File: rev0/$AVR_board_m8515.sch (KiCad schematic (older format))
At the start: 18 parts, among them IC1 ATMEGA8515-A, IC2 ATMEGA8515-M, K1 SERIAL, P1 FTDI_HEADER, P2 LEFT_HEADER, P3 CONN_3X2, P4 RIGHT_HEADER, SW1 SW_PUSH, X1 CRYSTAL_TH, X2 CRYSTAL_SMD

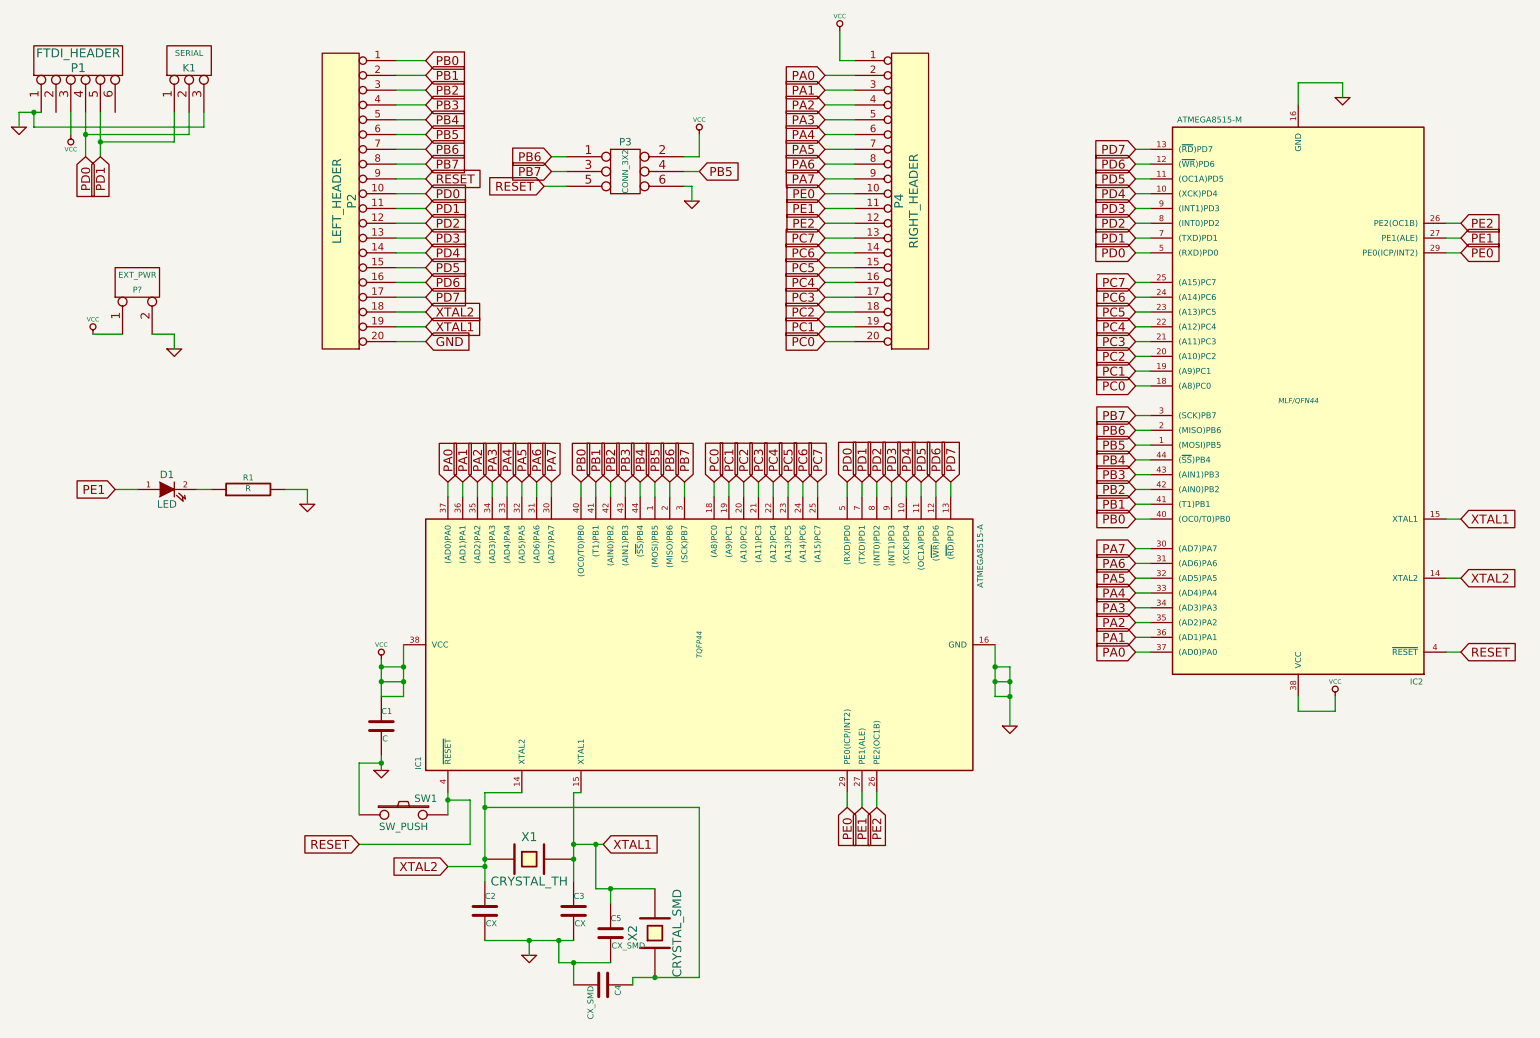
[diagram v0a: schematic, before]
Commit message: added logo mod file, also added silkscreen refs
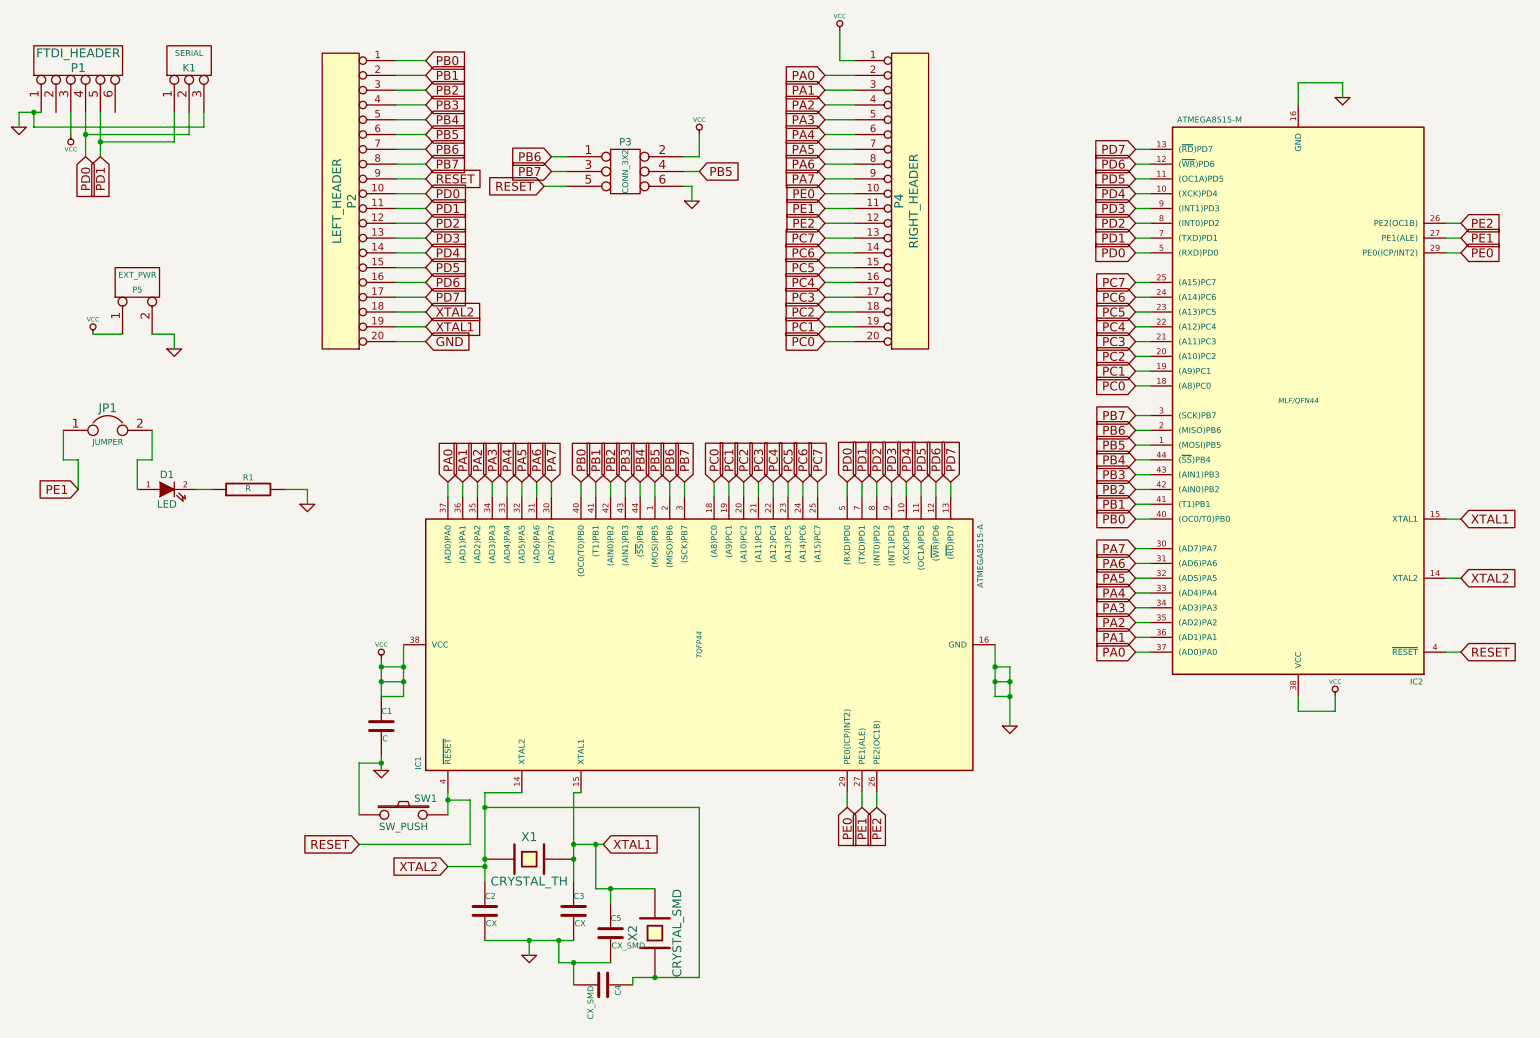
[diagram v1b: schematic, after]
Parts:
- added JP1: JUMPER, symbol JUMPER
- gave numbers to parts that had none: 1
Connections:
- net PE1: now also JP1.1; no longer D1.1 (A)
- new net: D1.1 (A), JP1.2
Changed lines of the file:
@@
 $EndComp
 $Comp
-L GND #PWR01
+L GND #PWR8
 U 1 1 54186B5E
 P 4500 7050
-F 0 "#PWR01" H 4500 7050 30  0001 C CNN
+F 0 "#PWR8" H 4500 7050 30  0001 C CNN
 F 1 "GND" H 4500 6980 30  0001 C CNN
 F 2 "" H 4500 7050 60  0000 C CNN
@@
 $EndComp
 $Comp
-L GND #PWR02
+L GND #PWR7
 U 1 1 54186C19
 P 3500 5800
-F 0 "#PWR02" H 3500 5800 30  0001 C CNN
+F 0 "#PWR7" H 3500 5800 30  0001 C CNN
 F 1 "GND" H 3500 5730 30  0001 C CNN
 F 2 "" H 3500 5800 60  0000 C CNN
@@
 $EndComp
 $Comp
-L VCC #PWR03
+L VCC #PWR6
 U 1 1 54186C37
 P 3500 5050
-F 0 "#PWR03" H 3500 5150 30  0001 C CNN
+F 0 "#PWR6" H 3500 5150 30  0001 C CNN
 F 1 "VCC" H 3500 5150 30  0000 C CNN
 F 2 "" H 3500 5050 60  0000 C CNN
@@
 	3500 5300 3650 5300
 $Comp
-L GND #PWR04
+L GND #PWR12
 U 1 1 54186C8C
 P 7750 5500
-F 0 "#PWR04" H 7750 5500 30  0001 C CNN
+F 0 "#PWR12" H 7750 5500 30  0001 C CNN
 F 1 "GND" H 7750 5430 30  0001 C CNN
 F 2 "" H 7750 5500 60  0000 C CNN
@@
 	7350 3850 7350 3950
 $Comp
-L VCC #PWR05
+L VCC #PWR11
 U 1 1 54189251
 P 6600 800
-F 0 "#PWR05" H 6600 900 30  0001 C CNN
+F 0 "#PWR11" H 6600 900 30  0001 C CNN
 F 1 "VCC" H 6600 900 30  0000 C CNN
 F 2 "" H 6600 800 60  0000 C CNN
@@
 $EndComp
 $Comp
-L GND #PWR06
+L GND #PWR14
 U 1 1 5418A680
 P 10000 1250
-F 0 "#PWR06" H 10000 1250 30  0001 C CNN
+F 0 "#PWR14" H 10000 1250 30  0001 C CNN
 F 1 "GND" H 10000 1180 30  0001 C CNN
 F 2 "" H 10000 1250 60  0000 C CNN
@@
 PA0
 $Comp
-L VCC #PWR07
+L VCC #PWR13
 U 1 1 5418A7C7
 P 9950 5300
-F 0 "#PWR07" H 9950 5400 30  0001 C CNN
+F 0 "#PWR13" H 9950 5400 30  0001 C CNN
 F 1 "VCC" H 9950 5400 30  0000 C CNN
 F 2 "" H 9950 5300 60  0000 C CNN
@@
 $EndComp
 $Comp
-L VCC #PWR08
+L VCC #PWR10
 U 1 1 5418C02E
 P 5650 1500
-F 0 "#PWR08" H 5650 1600 30  0001 C CNN
+F 0 "#PWR10" H 5650 1600 30  0001 C CNN
 F 1 "VCC" H 5650 1600 30  0000 C CNN
 F 2 "" H 5650 1500 60  0000 C CNN
@@
 PB5
 $Comp
-L GND #PWR09
+L GND #PWR9
 U 1 1 5418C0DE
 P 5600 1950
-F 0 "#PWR09" H 5600 1950 30  0001 C CNN
+F 0 "#PWR9" H 5600 1950 30  0001 C CNN
 F 1 "GND" H 5600 1880 30  0001 C CNN
 F 2 "" H 5600 1950 60  0000 C CNN
@@
 $EndComp
 Wire Wire Line
-	5350 6600 4950 6600
+	4950 6600 5350 6600
 Wire Wire Line
 	4950 6600 4950 6300
@@
 Connection ~ 5050 6600
 Wire Wire Line
-	5050 7100 4700 7100
+	4700 7100 5050 7100
 Wire Wire Line
 	4700 7100 4700 6950
@@
 	1    0    0    -1
 $EndComp
-Text GLabel 1700 3900 0    60   Input ~ 0
+Text GLabel 1450 3900 0    60   Input ~ 0
 PE1
 $Comp
@@
 $EndComp
 Wire Wire Line
-	1700 3900 1850 3900
-Wire Wire Line
 	2250 3900 2350 3900
 $Comp
-L GND #PWR010
+L GND #PWR5
 U 1 1 5418F076
 P 3000 4000
-F 0 "#PWR010" H 3000 4000 30  0001 C CNN
+F 0 "#PWR5" H 3000 4000 30  0001 C CNN
 F 1 "GND" H 3000 3930 30  0001 C CNN
 F 2 "" H 3000 4000 60  0000 C CNN
@@
 $EndComp
 $Comp
-L GND #PWR011
+L GND #PWR1
 U 1 1 5418F501
 P 1050 1450
-F 0 "#PWR011" H 1050 1450 30  0001 C CNN
+F 0 "#PWR1" H 1050 1450 30  0001 C CNN
 F 1 "GND" H 1050 1380 30  0001 C CNN
 F 2 "" H 1050 1450 60  0000 C CNN
@@
 $EndComp
 Wire Wire Line
-	1200 1350 1050 1350
+	1050 1350 1200 1350
 Wire Wire Line
 	1050 1350 1050 1450
 $Comp
-L VCC #PWR012
+L VCC #PWR2
 U 1 1 5418F6CA
 P 1400 1500
-F 0 "#PWR012" H 1400 1600 30  0001 C CNN
+F 0 "#PWR2" H 1400 1600 30  0001 C CNN
 F 1 "VCC" H 1400 1600 30  0000 C CNN
 F 2 "" H 1400 1500 60  0000 C CNN
@@
 Connection ~ 1150 1350
 $Comp
-L CONN_2 P?
+L CONN_2 P5
 U 1 1 54190E9B
 P 1850 2500
-F 0 "P?" V 1800 2500 40  0000 C CNN
+F 0 "P5" V 1800 2500 40  0000 C CNN
 F 1 "EXT_PWR" V 1900 2500 40  0000 C CNN
 F 2 "" H 1850 2500 60  0000 C CNN
@@
 $EndComp
 $Comp
-L VCC #PWR?
+L VCC #PWR3
 U 1 1 54190EB4
 P 1550 2850
-F 0 "#PWR?" H 1550 2950 30  0001 C CNN
+F 0 "#PWR3" H 1550 2950 30  0001 C CNN
 F 1 "VCC" H 1550 2950 30  0000 C CNN
 F 2 "" H 1550 2850 60  0000 C CNN
@@
 $EndComp
 $Comp
-L GND #PWR?
+L GND #PWR4
 U 1 1 54190EC3
 P 2100 2950
-F 0 "#PWR?" H 2100 2950 30  0001 C CNN
+F 0 "#PWR4" H 2100 2950 30  0001 C CNN
 F 1 "GND" H 2100 2880 30  0001 C CNN
 F 2 "" H 2100 2950 60  0000 C CNN
@@
 Wire Wire Line
 	1750 2850 1550 2850
+$Comp
+L JUMPER JP1
+U 1 1 54191199
+P 1650 3500
+F 0 "JP1" H 1650 3650 60  0000 C CNN
+F 1 "JUMPER" H 1650 3420 40  0000 C CNN
+F 2 "" H 1650 3500 60  0000 C CNN
+F 3 "" H 1650 3500 60  0000 C CNN
+	1    1650 3500
+	1    0    0    -1
+$EndComp
+Wire Wire Line
+	1950 3500 1950 3700
+Wire Wire Line
+	1950 3700 1850 3700
+Wire Wire Line
+	1850 3700 1850 3900
+Wire Wire Line
+	1350 3500 1350 3700
+Wire Wire Line
+	1350 3700 1450 3700
+Wire Wire Line
+	1450 3700 1450 3900
 $EndSCHEMATC
